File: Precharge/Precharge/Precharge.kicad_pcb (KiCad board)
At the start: 2 copper layers, 43 parts, among them J1 MicroFit, J2 ISP, J3 HV, J4 R_PRECHG, K1 OMRON-G2R-24, K2 G7L-2A-X-L, Q1 2N7002, Q2 2N7002, U1 AMS1117-5.0, U2 ATtiny85V-10SU, U3 MCP6562

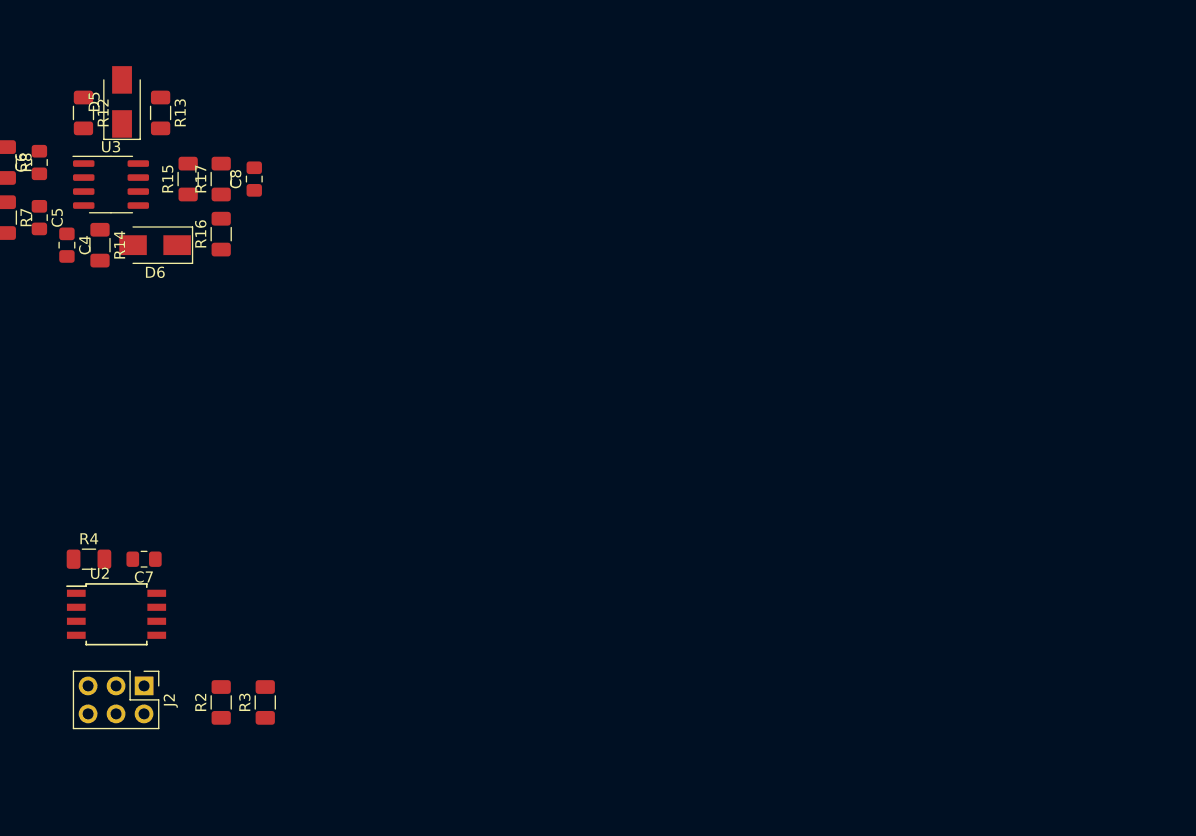
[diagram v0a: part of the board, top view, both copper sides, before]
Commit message: Update precharge design
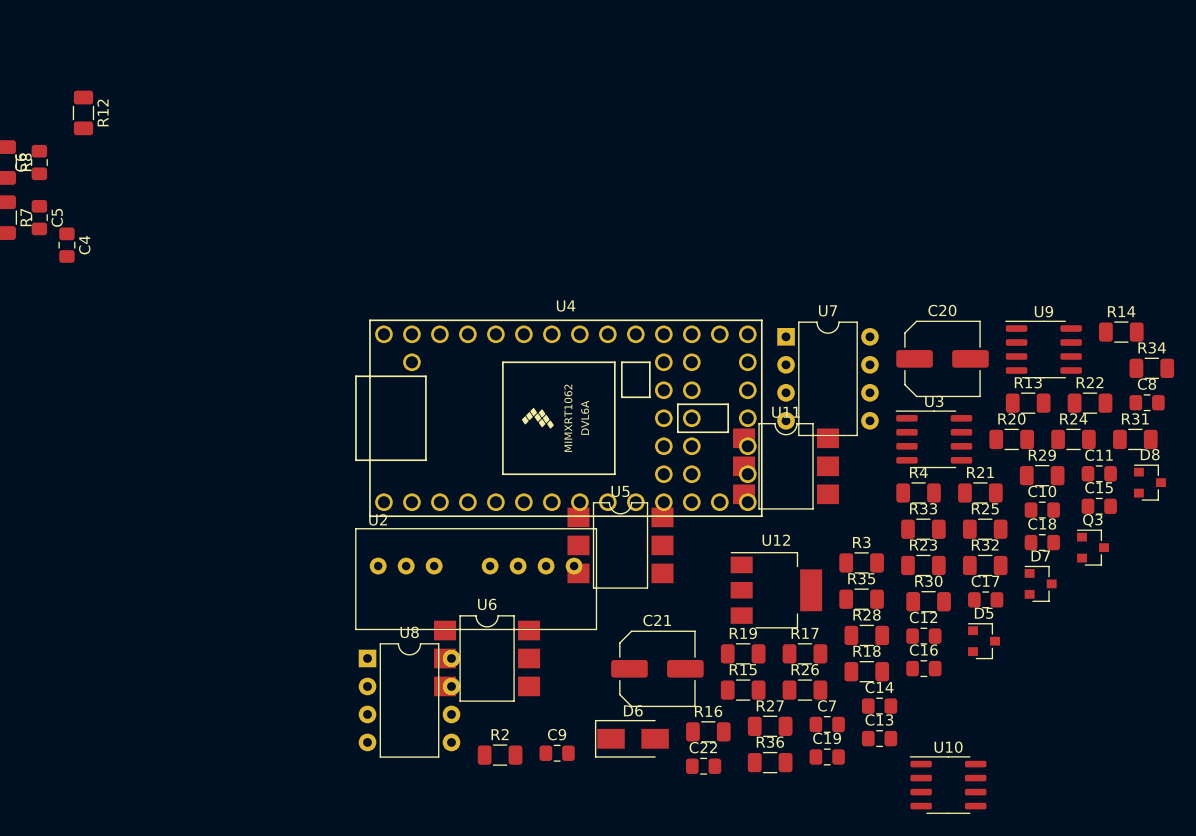
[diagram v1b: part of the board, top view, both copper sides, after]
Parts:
- removed J2: ISP, Connector_PinHeader_2.54mm:PinHeader_2x03_P2.54mm_Vertical
- added C10: 1u, Capacitor_SMD:C_0805_2012Metric_Pad1.15x1.40mm_HandSolder, F.Cu at (237.5, 119.5)
- added C11: 100n, Capacitor_SMD:C_0805_2012Metric_Pad1.15x1.40mm_HandSolder, F.Cu at (242.7, 116.2)
- added C12: 100n, Capacitor_SMD:C_0805_2012Metric_Pad1.15x1.40mm_HandSolder, F.Cu at (226.8, 131.0)
- added C13: 10n, Capacitor_SMD:C_0805_2012Metric_Pad1.15x1.40mm_HandSolder, F.Cu at (222.8, 140.3)
- added C14: 10n, Capacitor_SMD:C_0805_2012Metric_Pad1.15x1.40mm_HandSolder, F.Cu at (222.8, 137.3)
- added C15: 100n, Capacitor_SMD:C_0805_2012Metric_Pad1.15x1.40mm_HandSolder, F.Cu at (242.7, 119.2)
- added C16: 100n, Capacitor_SMD:C_0805_2012Metric_Pad1.15x1.40mm_HandSolder, F.Cu at (226.8, 133.9)
- added C17: 100n, Capacitor_SMD:C_0805_2012Metric_Pad1.15x1.40mm_HandSolder, F.Cu at (232.4, 127.7)
- added C18: 100n, Capacitor_SMD:C_0805_2012Metric_Pad1.15x1.40mm_HandSolder, F.Cu at (237.5, 122.5)
- added C19: 100n, Capacitor_SMD:C_0805_2012Metric_Pad1.15x1.40mm_HandSolder, F.Cu at (218.0, 141.9)
- added C20: 220u, Capacitor_SMD:C_Elec_6.3x5.4, F.Cu at (228.5, 105.8)
- added C21: 220u, Capacitor_SMD:C_Elec_6.3x5.4, F.Cu at (202.6, 133.9)
- added C22: 1u, Capacitor_SMD:C_0805_2012Metric_Pad1.15x1.40mm_HandSolder, F.Cu at (206.8, 142.8)
- added C9: 1u, Capacitor_SMD:C_0805_2012Metric_Pad1.15x1.40mm_HandSolder, F.Cu at (193.5, 141.6)
- added D7: BZX84Cxx, Diode_SMD:D_SOT-23_ANK, F.Cu at (237.4, 126.2)
- added D8: BZX84Cxx, Diode_SMD:D_SOT-23_ANK, F.Cu at (247.3, 117.0)
- added Q3: MMBT3906, Package_TO_SOT_SMD:SOT-23, F.Cu at (242.1, 123.0)
- added R18: 470, Resistor_SMD:R_1206_3216Metric, F.Cu at (221.6, 134.2)
- added R19: Rs, Resistor_SMD:R_1206_3216Metric, F.Cu at (210.4, 132.6)
- added R20: 47, Resistor_SMD:R_1206_3216Metric, F.Cu at (234.7, 113.1)
- added R21: 470, Resistor_SMD:R_1206_3216Metric, F.Cu at (231.9, 118.0)
- added R22: 6k8, Resistor_SMD:R_1206_3216Metric, F.Cu at (241.8, 109.8)
- added R23: 6k8, Resistor_SMD:R_1206_3216Metric, F.Cu at (226.7, 124.6)
- added R24: 100k, Resistor_SMD:R_1206_3216Metric, F.Cu at (240.3, 113.1)
- added R25: 100k, Resistor_SMD:R_1206_3216Metric, F.Cu at (232.3, 121.3)
- added R26: 500k, Resistor_SMD:R_1206_3216Metric, F.Cu at (216.0, 135.9)
- added R27: 500k, Resistor_SMD:R_1206_3216Metric, F.Cu at (212.8, 139.2)
- added R28: 500k, Resistor_SMD:R_1206_3216Metric, F.Cu at (221.6, 130.9)
- added R29: 500k, Resistor_SMD:R_1206_3216Metric, F.Cu at (237.5, 116.4)
- added R30: 40k, Resistor_SMD:R_1206_3216Metric, F.Cu at (227.2, 127.9)
- added R31: 500k, Resistor_SMD:R_1206_3216Metric, F.Cu at (246.0, 113.1)
- added R32: 500k, Resistor_SMD:R_1206_3216Metric, F.Cu at (232.3, 124.6)
- added R33: 500k, Resistor_SMD:R_1206_3216Metric, F.Cu at (226.7, 121.3)
- added R34: 500k, Resistor_SMD:R_1206_3216Metric, F.Cu at (247.5, 106.7)
- added R35: 40k, Resistor_SMD:R_1206_3216Metric, F.Cu at (221.1, 127.6)
- added R36: 10k, Resistor_SMD:R_1206_3216Metric, F.Cu at (212.8, 142.5)
- added U10: LM311, Package_SO:SOIC-8_3.9x4.9mm_P1.27mm, F.Cu at (229.0, 144.5)
- added U11: 4N35, Package_DIP:SMDIP-6_W7.62mm, F.Cu at (214.3, 115.6)
- added U12: AMS1117-5.0, Package_TO_SOT_SMD:SOT-223-3_TabPin2, F.Cu at (213.4, 126.8)
- added U4: Teensy4.0, teensy:Teensy40, F.Cu at (194.3, 111.2)
- added U5: 4N35, Package_DIP:SMDIP-6_W7.62mm, F.Cu at (199.2, 122.8)
- added U6: 4N35, Package_DIP:SMDIP-6_W7.62mm, F.Cu at (187.1, 133.0)
- added U7: LM331, Package_DIP:DIP-8_W7.62mm, F.Cu at (214.3, 103.8)
- added U8: LM331, Package_DIP:DIP-8_W7.62mm, F.Cu at (176.3, 133.0)
- added U9: LM2904, Package_SO:SOIC-8_3.9x4.9mm_P1.27mm, F.Cu at (237.7, 105.0)
- C7: value 100n -> 1u
- D5: value D -> BZX84Cxx; footprint Diode_SMD:D_SMA -> Diode_SMD:D_SOT-23_ANK
- R12: value 100 -> 470
- R13: value 100 -> 47
- R14: value 10k -> 20k
- R15: value 10k -> 7k
- R16: value 10k -> 500k
- R17: value 10k -> 100
- R2, R3: value 100k -> 1k
- R4: value 10k -> Rs
- U1: value AMS1117-5.0 -> LM1117-5.0
- U2: value ATtiny85V-10SU -> SPAN02A-12; footprint Package_SO:SOIJ-8_5.3x5.3mm_P1.27mm -> Precharge:SPAN02
- moved R14 93.0 mm to (244.7, 103.4), turned to 0 degrees
- moved D5 92.3 mm to (232.2, 131.4), turned to 0 degrees
- moved C8 83.5 mm to (247.0, 109.8), turned to 0 degrees
- moved R13 83.0 mm to (236.2, 109.8), turned to 0 degrees
- moved U3 78.2 mm to (227.7, 113.1)
- moved R4 75.5 mm to (226.3, 118.0)
- moved R15 68.5 mm to (210.4, 135.9), turned to 0 degrees
- moved R17 68.3 mm to (216.0, 132.6), turned to 0 degrees
- moved C7 63.8 mm to (218.0, 139.0), turned to 0 degrees
- moved R16 63.2 mm to (207.2, 139.7), turned to 0 degrees
- moved D6 62.4 mm to (200.4, 140.3), turned to 0 degrees
- moved R3 55.6 mm to (221.1, 124.3), turned to 0 degrees
- moved U2 32.5 mm to (185.9, 125.8)
- moved R2 25.8 mm to (188.3, 141.8), turned to 0 degrees
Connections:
- net /HV_IN renamed Net-(J3-Pad1)
- net /HV_OUT renamed /VinAccu
- net /V_TS renamed /VinTS
- C4 pad 1: +5V -> +5P
- C4 pad 2: GLV- -> GNDS
- C5 pad 2: GLV- -> GNDS
- C6 pad 2: GLV- -> GNDS
- C7 pad 1: GLV- -> GNDS
- C7 pad 2: +5V -> +12P
- D5 pad 1: Net-(D5-Pad1) -> Net-(C18-Pad1)
- D5 pad 2: Net-(D5-Pad2) -> GNDS
- J1 pad 5: /PDOC -> /PDOC_OK
- R10 pad 1: /PRECHG -> (no net)
- R12 pad 1: /PDOC -> Net-(R12-Pad1)
- R13 pad 1: /~RESET -> GNDS
- R13 pad 2: Net-(D5-Pad2) -> Net-(C9-Pad1)
- R14 pad 1: +5V -> Net-(D6-Pad1)
- R14 pad 2: Net-(R14-Pad2) -> Net-(C8-Pad1)
- R15 pad 1: Net-(R14-Pad2) -> Net-(C8-Pad1)
- R16 pad 1: Net-(D6-Pad1) -> Net-(R12-Pad2)
- R16 pad 2: Net-(C8-Pad1) -> Net-(C5-Pad1)
- R17 pad 1: Net-(C8-Pad1) -> Net-(R17-Pad1)
- R17 pad 2: GLV- -> Net-(Q3-Pad1)
- R2 pad 1: +5V -> GLV-
- R2 pad 2: /MISO -> /Fts
- R3 pad 1: +5V -> GLV-
- R3 pad 2: /SCK -> /Faccu
- R4 pad 1: /~RESET -> GNDS
- R4 pad 2: +5V -> Net-(R4-Pad2)
- R5 pad 2: /SHTDN_CTRL -> (no net)
- R7 pad 1: Net-(C5-Pad1) -> +12P
- R7 pad 2: GLV- -> Net-(C5-Pad1)
- R8 pad 1: +5V -> Net-(C5-Pad1)
- R8 pad 2: Net-(C6-Pad1) -> GNDS
- R9 pad 2: GLV- -> GNDS
- TH1 pad 1: Net-(C5-Pad1) -> Net-(C6-Pad1)
- TH1 pad 2: +5V -> +12P
- U2 pad 1: /~RESET -> GLV-
- U2 pad 2: /PRECHG -> +12V
- U2 pad 3: /SHTDN_CTRL -> (no net)
- U2 pad 5: /MOSI -> (no net)
- U2 pad 6: /MISO -> +12P
- U2 pad 7: /SCK -> GNDS
- U2 pad 8: +5V -> (no net)
- U3 pad 1: Net-(R12-Pad2) -> (no net)
- U3 pad 2: Net-(C6-Pad1) -> (no net)
- U3 pad 3: Net-(C5-Pad1) -> (no net)
- U3 pad 4: +5V -> GNDS
- U3 pad 5: Net-(C8-Pad1) -> GNDS
- U3 pad 6: Net-(R14-Pad2) -> +5P
- U3 pad 7: Net-(D5-Pad1) -> (no net)
- U3 pad 8: GLV- -> +5P

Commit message: update precharge schematic + pcb
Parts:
- removed the C2 at (114.5, 107.5)
- removed the D8 at (247.3, 117.0)
- removed J3: HV, Connector_Molex:Molex_Mini-Fit_Jr_5566-02A_2x01_P4.20mm_Vertical
- removed J4: R_PRECHG, Connector_Molex:Molex_Mini-Fit_Jr_5566-02A_2x01_P4.20mm_Vertical
- removed the R13 at (236.2, 109.8)
- removed the R22 at (241.8, 109.8)
- removed the R25 at (232.3, 121.3)
- removed the R26 at (216.0, 135.9)
- removed the R34 at (247.5, 106.7)
- removed the U10 at (229.0, 144.5)
- removed U12: AMS1117-5.0, Package_TO_SOT_SMD:SOT-223-3_TabPin2
- removed the U3 at (227.7, 113.1)
- removed the U4 at (194.3, 111.2)
- removed the U7 at (214.3, 103.8)
- added C6: 220u, Capacitor_SMD:C_Elec_6.3x5.4, F.Cu at (134.0, 112.0)
- added D2: LED, LED_SMD:LED_0805_2012Metric_Castellated, F.Cu at (154.5, 155.7)
- added D3: LED, LED_SMD:LED_0805_2012Metric_Castellated, F.Cu at (147.4, 163.8)
- added D4: LED, LED_SMD:LED_0805_2012Metric_Castellated, F.Cu at (153.0, 159.0)
- added D5: LED, LED_SMD:LED_0805_2012Metric_Castellated, F.Cu at (160.1, 152.4)
- added D6: BZX84C3V3, Diode_SMD:D_SOT-23_ANK, F.Cu at (247.3, 117.0)
- added J2: HV, Connector_Molex:Molex_Mini-Fit_Jr_5566-02A_2x01_P4.20mm_Vertical, F.Cu at (396.0, 122.0)
- added JP1: SolderJumper_2_Open, Jumper:SolderJumper-2_P1.3mm_Open_RoundedPad1.0x1.5mm, F.Cu at (152.8, 162.2)
- added JP2: SolderJumper_2_Open, Jumper:SolderJumper-2_P1.3mm_Open_RoundedPad1.0x1.5mm, F.Cu at (157.6, 158.9)
- added JP3: SolderJumper_2_Open, Jumper:SolderJumper-2_P1.3mm_Open_RoundedPad1.0x1.5mm, F.Cu at (157.1, 162.5)
- added R1: 200, Resistor_SMD:R_1206_3216Metric, F.Cu at (149.3, 152.6)
- added R10: Rs, Resistor_SMD:R_1206_3216Metric, F.Cu at (308.0, 150.0)
- added R11: 47, Resistor_SMD:R_1206_3216Metric, F.Cu at (324.0, 155.0)
- added R12: 470, Resistor_SMD:R_1206_3216Metric, F.Cu at (308.0, 154.0)
- added R2: 200, Resistor_SMD:R_1206_3216Metric, F.Cu at (149.3, 155.9)
- added R23: 100k, Resistor_SMD:R_1206_3216Metric, F.Cu at (339.5, 158.0)
- added R3: 200, Resistor_SMD:R_1206_3216Metric, F.Cu at (147.8, 160.7)
- added R31: 500k, Resistor_SMD:R_1206_3216Metric, F.Cu at (355.0, 166.0)
- added R32: 40k, Resistor_SMD:R_1206_3216Metric, F.Cu at (350.0, 164.0)
- added R33: 500k, Resistor_SMD:R_1206_3216Metric, F.Cu at (369.0, 133.0)
- added R37: 500k, Resistor_SMD:R_1206_3216Metric, F.Cu at (355.0, 147.0)
- added R43: R, Precharge:Chassis_Resistor_TE_Connectivity_HSA25, F.Cu at (386.5, 156.5)
- added TP1: TestPoint, TestPoint:TestPoint_Loop_D2.50mm_Drill1.0mm_LowProfile, F.Cu at (299.5, 116.5)
- added TP2: TestPoint, TestPoint:TestPoint_Loop_D2.50mm_Drill1.0mm_LowProfile, F.Cu at (301.0, 110.0)
- added TP3: TestPoint, TestPoint:TestPoint_Loop_D2.50mm_Drill1.0mm_LowProfile, F.Cu at (349.0, 168.0)
- added TP4: TestPoint, TestPoint:TestPoint_Loop_D2.50mm_Drill1.0mm_LowProfile, F.Cu at (349.0, 145.0)
- added U2: Teensy4.0, teensy:Teensy40, F.Cu at (86.5, 193.0)
- added U6: LM331, Package_DIP:DIP-8_W7.62mm, F.Cu at (313.0, 148.0)
- added U8: LM2904, Package_SO:SOIC-8_3.9x4.9mm_P1.27mm, F.Cu at (352.0, 156.5)
- C22: value 1u -> 100n
- C4: value 100n -> 220u; footprint Capacitor_SMD:C_0805_2012Metric_Pad1.15x1.40mm_HandSolder -> Capacitor_SMD:C_Elec_6.3x5.4
- D10: renamed from D5; value BZX84Cxx -> BZX84C12
- D11: renamed from D7; value BZX84Cxx -> BZX84C12
- R18: value 470 -> 6k8
- R30: value 40k -> 500k
- R4: value Rs -> 200
- U9: value LM2904 -> LM393
- moved K2 355.4 mm to (429.5, 173.0), turned to 90 degrees
- moved R27 161.4 mm to (369.0, 180.0), turned to 135 degrees
- moved R28 151.0 mm to (365.5, 176.5), turned to 135 degrees
- moved U7 141.1 mm to (313.0, 168.0)
- moved R30 137.7 mm to (358.5, 169.5), turned to 135 degrees
- moved R29 136.7 mm to (362.0, 173.0), turned to 135 degrees
- moved R36 133.6 mm to (358.5, 143.5), turned to 225 degrees
- moved R38 130.6 mm to (350.0, 149.0), turned to 180 degrees
- moved R35 130.6 mm to (362.0, 140.0), turned to 225 degrees
- moved C21 127.4 mm to (345.0, 152.5), turned to 180 degrees
- moved C9 123.6 mm to (317.0, 145.0), turned to 180 degrees
- moved R34 121.8 mm to (365.5, 136.5), turned to 225 degrees
- moved D10 117.2 mm to (345.0, 163.5)
- moved C20 114.0 mm to (345.0, 160.5), turned to 180 degrees
- moved U9 112.6 mm to (140.8, 162.3)
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- renumbered C8 to C1, C5 to C18, C6 to C19, C1 to C2, C18 to C20, C19 to C21, C7 to C3, C20 to C5, C21 to C7, C3 to C8, D6 to D1, D4 to D12, D1 to D7, D2 to D8, D3 to D9, Q3 to Q2, Q2 to Q3, R19 to R13, R20 to R14, R21 to R15, R5 to R16, R6 to R17, R23 to R19, R24 to R20, R7 to R21, R8 to R22, R9 to R24, R16 to R25, R12 to R26, R31 to R34, R32 to R35, R33 to R36, R35 to R38, R17 to R39, R36 to R40, R10 to R41, R11 to R42, R14 to R5, R15 to R6, R1 to R7, R2 to R8, R3 to R9, U2 to U1, U11 to U10, U1 to U3, U5 to U4, U6 to U5, U8 to U7
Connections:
- net Net-(C8-Pad1) renamed /PWR_OK
- C18 pad 1: Net-(C5-Pad1) -> Net-(C18-Pad1)
- C19 pad 1: Net-(C6-Pad1) -> Net-(C19-Pad1)
- C20 pad 1: Net-(C18-Pad1) -> Net-(C20-Pad1)
- C21 pad 1: Net-(C19-Pad1) -> Net-(C21-Pad1)
- C22 pad 1: +5P -> +12P
- C4 pad 1: +5P -> +12V
- C4 pad 2: GNDS -> GLV-
- D10 pad 1: Net-(C18-Pad1) -> Net-(C20-Pad1)
- D11 pad 1: Net-(C19-Pad1) -> Net-(C21-Pad1)
- R18 pad 1: /FoutTS -> Net-(C13-Pad1)
- R18 pad 2: Net-(R18-Pad2) -> +12P
- R20 pad 1: /VinTS -> Net-(R20-Pad1)
- R21 pad 2: Net-(C5-Pad1) -> Net-(C18-Pad1)
- R22 pad 1: Net-(C5-Pad1) -> Net-(C18-Pad1)
- R24 pad 1: Net-(C6-Pad1) -> Net-(C19-Pad1)
- R25 pad 1: Net-(R12-Pad2) -> Net-(R25-Pad1)
- R25 pad 2: Net-(C5-Pad1) -> Net-(C18-Pad1)
- R26 pad 2: Net-(R12-Pad2) -> Net-(R25-Pad1)
- R27 pad 1: Net-(R26-Pad2) -> /VinAccu
- R29 pad 2: Net-(C18-Pad1) -> Net-(R29-Pad2)
- R30 pad 1: Net-(C18-Pad1) -> Net-(R29-Pad2)
- R30 pad 2: GNDS -> Net-(R30-Pad2)
- R34 pad 1: /VinTS -> Net-(R33-Pad2)
- R38 pad 1: Net-(C19-Pad1) -> Net-(C21-Pad1)
- R4 pad 1: GNDS -> Net-(D5-Pad1)
- R4 pad 2: Net-(R4-Pad2) -> GLV-
- TH1 pad 1: Net-(C6-Pad1) -> Net-(C19-Pad1)
- U9 pad 2: Net-(R25-Pad1) -> Net-(C19-Pad1)
- U9 pad 5: Net-(C19-Pad1) -> GNDS
- U9 pad 6: /VinTS -> +12P
- U9 pad 7: /VinTS -> (no net)

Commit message: :hammer: Precharge:arrange components
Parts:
- added R44: 20k, Resistor_SMD:R_1206_3216Metric, F.Cu at (191.5, 134.0)
- added R45: 7k, Resistor_SMD:R_1206_3216Metric, F.Cu at (191.5, 136.5)
- R1, R2, R3, R4: moved to B.Cu
- R39: value 100 -> 470
- moved J2 293.1 mm to (110.0, 58.0), turned to 270 degrees
- moved TP3 283.7 mm to (78.0, 84.0)
- moved TP4 280.5 mm to (76.5, 78.5)
- moved R43 270.7 mm to (127.0, 79.5), turned to 0 degrees
- moved R33 266.0 mm to (105.5, 96.4), turned to 270 degrees
- moved R34 262.4 mm to (105.5, 101.3), turned to 270 degrees
- moved TP1 261.6 mm to (49.5, 39.5)
- moved TP2 261.6 mm to (51.0, 33.0)
- moved K2 259.0 mm to (181.0, 100.0)
- moved R35 256.7 mm to (107.5, 106.2), turned to 315 degrees
- moved R36 248.6 mm to (112.4, 108.2), turned to 0 degrees
- moved R37 240.8 mm to (117.4, 108.2), turned to 0 degrees
- moved R30 235.2 mm to (134.9, 96.5), turned to 180 degrees
- moved R27 235.1 mm to (150.0, 94.5), turned to 225 degrees
- moved R31 234.9 mm to (130.0, 98.5), turned to 225 degrees
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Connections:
- D2 pad 2: (no net) -> Net-(D2-Pad2)
- D3 pad 2: (no net) -> Net-(D3-Pad2)
- D4 pad 2: (no net) -> Net-(D4-Pad2)
- D5 pad 2: (no net) -> Net-(D5-Pad2)
- U2 pad 2: (no net) -> Net-(D2-Pad2)
- U2 pad 28: (no net) -> Net-(R44-Pad2)
- U2 pad 3: (no net) -> Net-(D3-Pad2)
- U2 pad 4: (no net) -> Net-(D4-Pad2)
- U2 pad 5: (no net) -> Net-(D5-Pad2)
